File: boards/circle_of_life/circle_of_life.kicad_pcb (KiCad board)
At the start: 2 copper layers, 100 x 82 mm, 110 parts, among them IC1 ESP32-WROOM-32E-N8R2, IC2 TC1262-3.3VDB, IC3 TPS565242DRLR, IC4 LT3922EUFD#PBF, IC5 TXU0101DBVR, J1 Water Pump Connector, J11 LED Connector, J2 Servo Motor Connector, J3 Power Connector, J4 pH Sensor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

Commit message: slightly modified it
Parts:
- moved LED6 204.1 mm to (66.7, 91.8)
- moved LED1 202.9 mm to (66.7, 98.0), turned to 180 degrees
- moved LED7 194.4 mm to (74.5, 91.8)
- moved LED3 189.1 mm to (74.5, 98.0)
- moved LED8 184.9 mm to (82.0, 91.8)
- moved LED9 179.7 mm to (89.5, 98.0), turned to 180 degrees
- moved LED2 178.4 mm to (89.5, 91.8)
- moved LED5 175.5 mm to (81.9, 98.0), turned to 180 degrees
- moved LED10 170.0 mm to (97.2, 98.0), turned to 180 degrees
- moved LED4 164.5 mm to (97.2, 91.8), turned to 180 degrees
- moved J9 53.8 mm to (246.4, 121.0), turned to -90 degrees
- moved IC2 45.8 mm to (194.8, 84.8), turned to 90 degrees
- moved R25 42.8 mm to (187.2, 104.4), turned to 90 degrees
- moved C1 40.0 mm to (193.0, 90.5), turned to 0 degrees
- moved R24 39.3 mm to (189.2, 106.4), turned to 90 degrees
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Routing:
- net +12V: track 0.00 -> 8.67 mm
- net Net-(IC4-PWMTG): track 19.5 -> 25.9 mm
- net ISP: track 9.24 -> 14.0 mm
- net Net-(IC4-CTRL): track 0.50 -> 3.83 mm
- net ISN: track 9.24 -> 11.7 mm
- net INTV: track 5.49 -> 3.71 mm
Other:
- board size 100 x 82 mm -> 100 x 75 mm

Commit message: added usb-uart programmer so that its easier to program :D
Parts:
- added C44: 4.7uF, Capacitor_SMD:C_0805_2012Metric, F.Cu at (222.1, 137.3)
- added C45: 0.1uF, Capacitor_SMD:C_0603_1608Metric, F.Cu at (210.6, 137.1)
- added C46: 4.7uF, Capacitor_SMD:C_0805_2012Metric, F.Cu at (222.1, 140.3)
- added C47: 0.1uF, Capacitor_SMD:C_0603_1608Metric, F.Cu at (210.6, 139.6)
- added D10: LED, LED_SMD:LED_0603_1608Metric, F.Cu at (225.6, 151.4)
- added D8: SP0503BAHTG, SamacSys_Parts:SP0503BAHTG, F.Cu at (220.5, 150.9)
- added D9: LED, LED_SMD:LED_0603_1608Metric, F.Cu at (225.6, 148.8)
- added IC6: CP2102C-A01-GQFN28, SamacSys_Parts:QFN50P500X500X80-29N-D, F.Cu at (216.2, 139.4)
- added P1: USB_C_Plug_USB2.0, Connector_USB:USB_C_Receptacle_GCT_USB4125-xx-x_6P_TopMnt_Horizontal, F.Cu at (234.0, 141.2)
- added Q3: SS8050, Package_TO_SOT_SMD:SOT-23, F.Cu at (215.1, 149.8)
- added Q4: SS8050, Package_TO_SOT_SMD:SOT-23, F.Cu at (215.1, 154.2)
- added R29: 22.1k, Resistor_SMD:R_0603_1608Metric, F.Cu at (210.6, 142.1)
- added R30: 47.5k, Resistor_SMD:R_0603_1608Metric, F.Cu at (210.6, 144.6)
- added R31: 22.1k, Resistor_SMD:R_0603_1608Metric, F.Cu at (210.6, 147.1)
- added R32: 10k, Resistor_SMD:R_0603_1608Metric, F.Cu at (210.6, 149.6)
- added R33: 5.1k, Resistor_SMD:R_0603_1608Metric, F.Cu at (210.6, 152.1)
- added R34: 1k, SamacSys_Parts:RESC1608X55N, F.Cu at (225.5, 154.0)
- added R35: 1k, SamacSys_Parts:RESC1608X55N, F.Cu at (225.5, 156.5)
- added R36: 10k, Resistor_SMD:R_0603_1608Metric, F.Cu at (210.6, 154.6)
- added R37: 10k, Resistor_SMD:R_0603_1608Metric, F.Cu at (210.6, 157.1)
- C24: footprint Capacitor_SMD:C_0603_1608Metric -> SamacSys_Parts:C0603

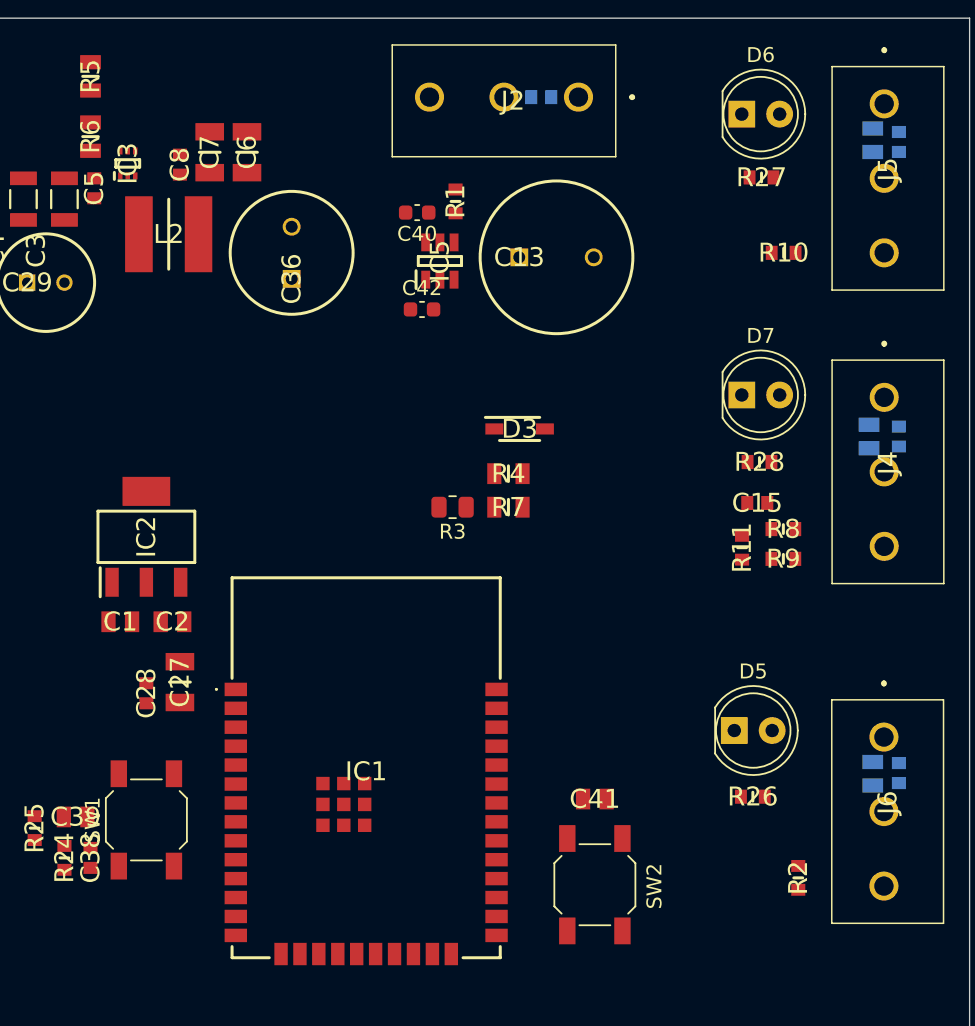
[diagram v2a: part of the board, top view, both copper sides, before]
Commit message: 5V signal routing done
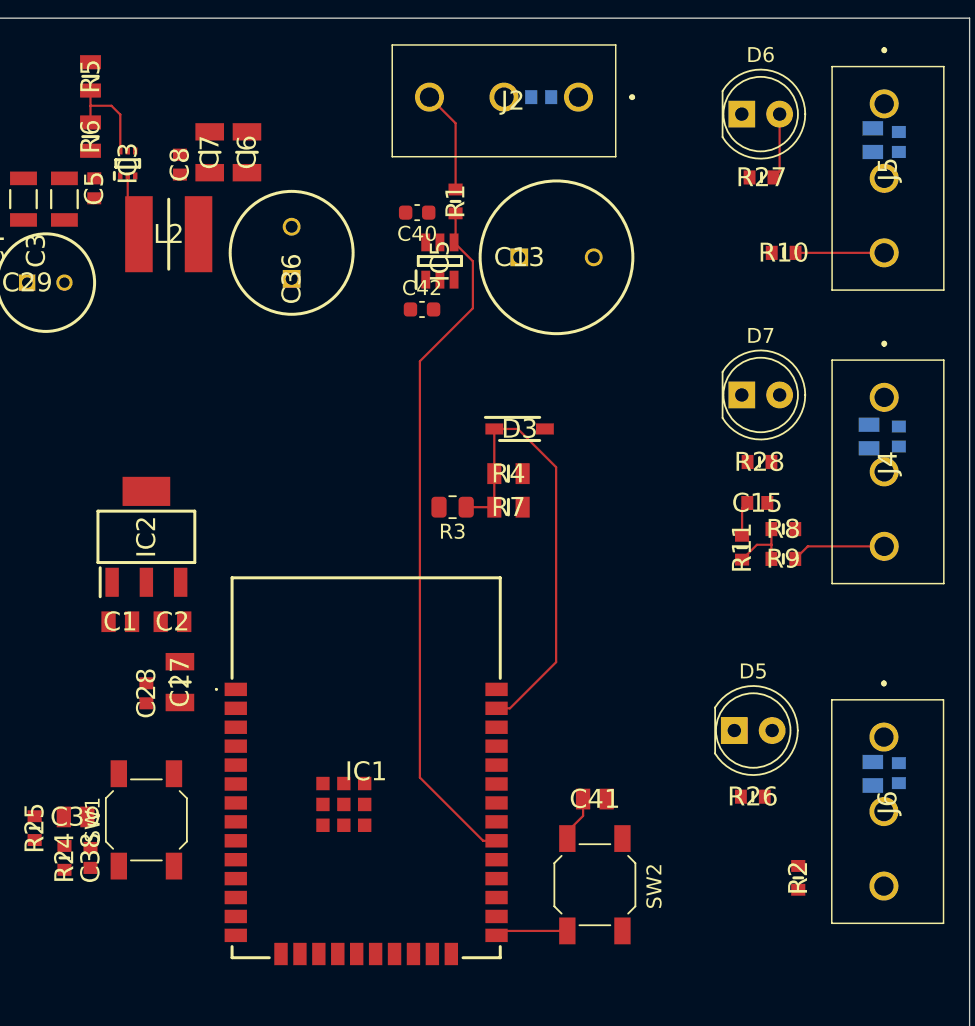
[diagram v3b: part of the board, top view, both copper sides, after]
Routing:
- net SRV_SGN: track 0.00 -> 46.8 mm
- net EN: track 0.00 -> 30.7 mm
- net IO0: track 0.00 -> 7.96 mm
- net Net-(J2-Pin_3): track 0.00 -> 6.92 mm
- net Net-(IC3-FB): track 0.00 -> 6.83 mm
- net PH_SGN: track 0.00 -> 6.32 mm
- net FLOW_SGN: track 0.00 -> 5.95 mm
- net Net-(R11-Pad1): track 0.00 -> 4.45 mm
- net Net-(D6-A): track 0.00 -> 4.42 mm
- net Net-(IC3-SW): track 0.00 -> 4.22 mm
- net PH_SGN_3.3V: track 0.00 -> 2.34 mm

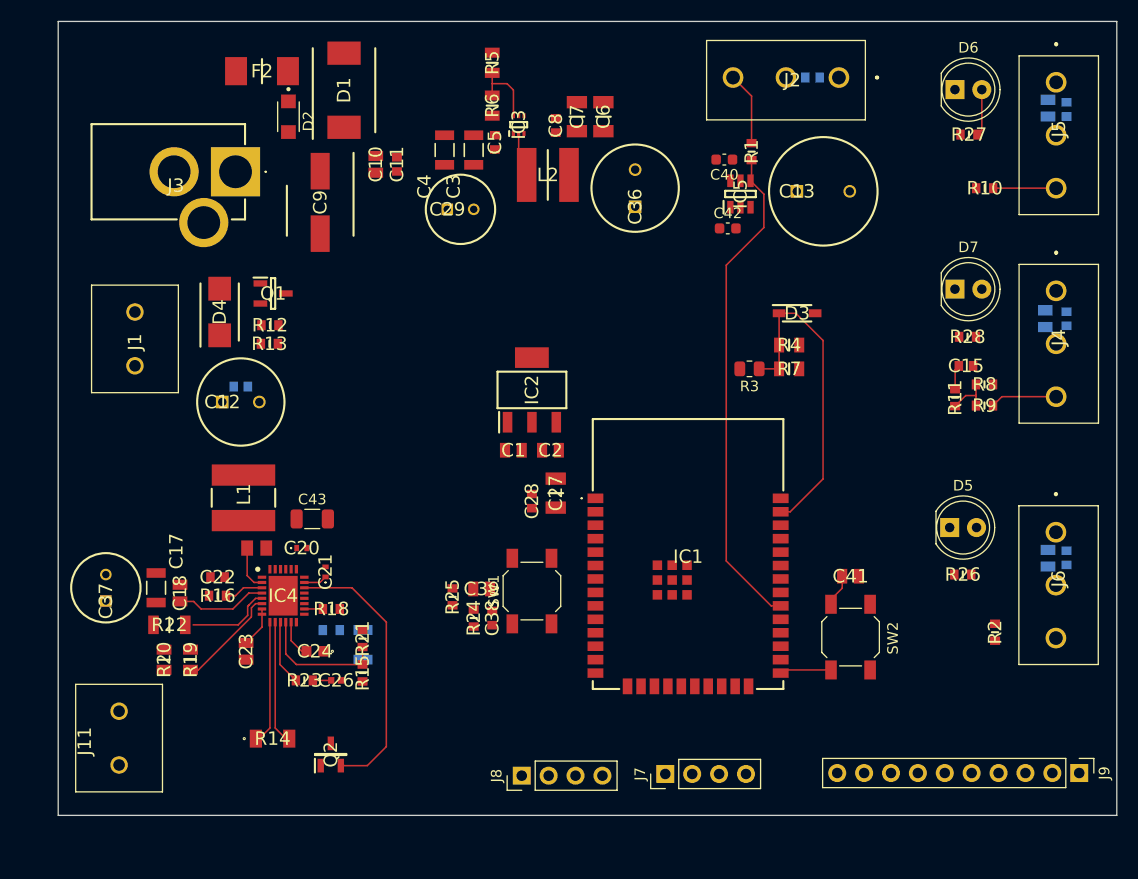
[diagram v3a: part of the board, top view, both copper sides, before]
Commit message: mcu connections started
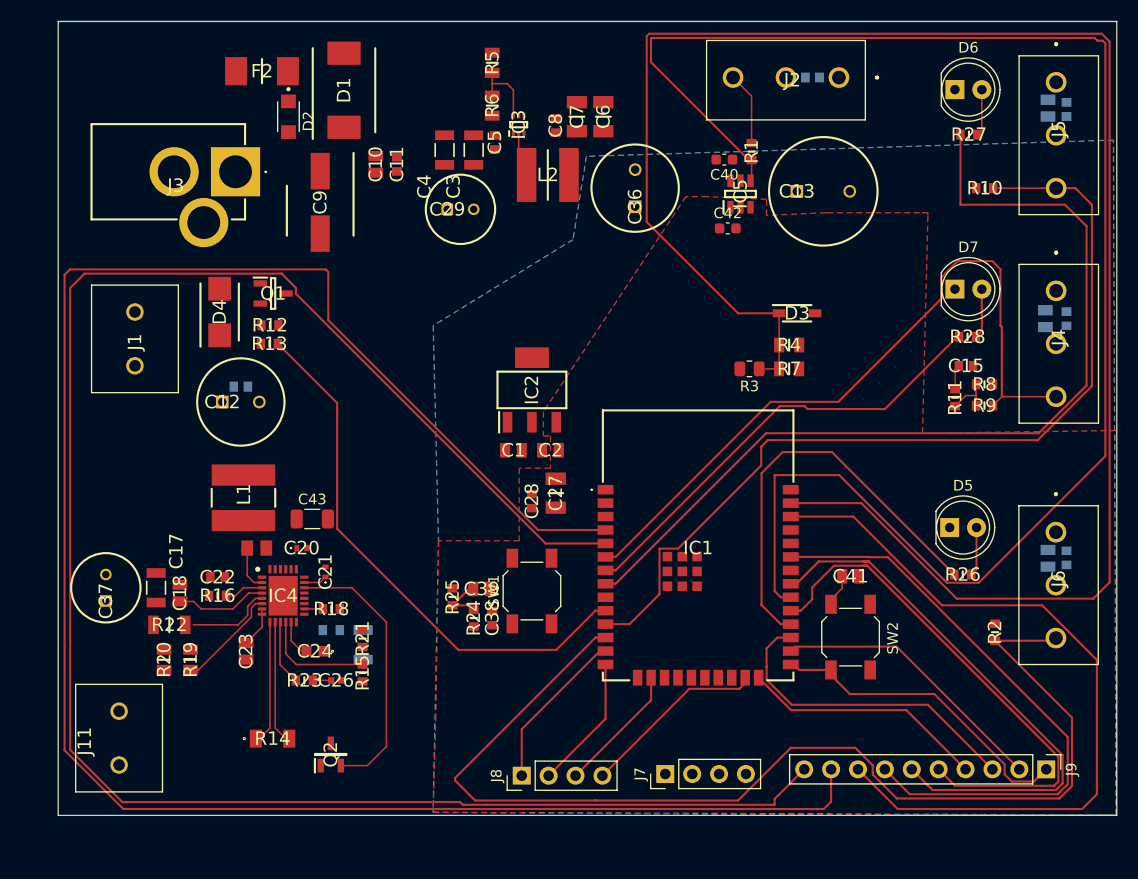
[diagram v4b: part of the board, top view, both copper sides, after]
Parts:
- moved J9 3.14 mm to (243.3, 120.7)
- moved IC1 1.25 mm to (210.5, 99.5)
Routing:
- net SENSOR_VP: track 0.00 -> 188.9 mm
- net SENSOR_VIN: track 0.00 -> 180.0 mm
- net EN: track 30.7 -> 170.5 mm
- net TMP_SGN: track 0.00 -> 106.7 mm
- net SRV_SGN: track 46.8 -> 153.0 mm
- net FLOW_FAULT: track 0.00 -> 87.6 mm
- net FLOW_SGN: track 5.95 -> 85.9 mm
- net IO22: track 0.00 -> 71.9 mm
- net PH_SGN: track 6.32 -> 68.9 mm
- net IO21: track 0.00 -> 56.6 mm
- net IO19: track 0.00 -> 52.9 mm
- net PUMP_SGN: track 0.00 -> 51.4 mm
- net IO5: track 0.00 -> 50.0 mm
- net TEMP_FAULT: track 0.00 -> 42.8 mm
- net PH_FAULT: track 0.00 -> 39.8 mm
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- added copper zone on F.Cu, net +3.3V
- added copper zone on B.Cu, net GND

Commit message: modified layout rip
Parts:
- removed C46: 4.7uF, Capacitor_SMD:C_0805_2012Metric
- removed C47: 0.1uF, Capacitor_SMD:C_0603_1608Metric
- removed J9: Conn_01x10_Pin, Connector_PinHeader_2.54mm:PinHeader_1x10_P2.54mm_Vertical
- removed LED1, LED10, LED3, LED5, LED9: ASMW-LL00-NKM0E, SamacSys_Parts:ASMWLL00NKM0E
- removed LED2, LED4, LED6, LED7, LED8: ASMW-LD00-AGJ0E, SamacSys_Parts:ASMWL300AFH0E
- added D11: TPD1E05U06QDPYRQ1, SamacSys_Parts:DPY_R-PX1SON-N2_, F.Cu at (105.6, 155.7)
- added R38: 0, Resistor_SMD:R_0603_1608Metric, F.Cu at (112.2, 145.7)
- added R39: 0, Resistor_SMD:R_0603_1608Metric, F.Cu at (113.9, 145.7)
- C22, R16, R2: moved to B.Cu
- C24: footprint SamacSys_Parts:C0603 -> Capacitor_SMD:C_0603_1608Metric
- D8: value SP0503BAHTG -> TPD1E05U06QDPYRQ1; footprint SamacSys_Parts:SP0503BAHTG -> SamacSys_Parts:DPY_R-PX1SON-N2_
- P1: footprint Connector_USB:USB_C_Receptacle_GCT_USB4125-xx-x_6P_TopMnt_Horizontal -> Connector_USB:USB_C_Receptacle_HRO_TYPE-C-31-M-12
- moved J5 192.4 mm to (110.6, 194.2), turned to 0 degrees
- moved J2 191.5 mm to (92.0, 194.3), turned to 0 degrees
- moved C32 190.9 mm to (112.8, 195.8), turned to 180 degrees
- moved C14 188.1 mm to (94.5, 194.3), turned to 180 degrees
- moved C33 187.0 mm to (112.7, 191.8), turned to 180 degrees
- moved J4 180.2 mm to (92.1, 171.9), turned to 90 degrees
- moved C31 179.1 mm to (91.1, 169.3), turned to -90 degrees
- moved D6 178.5 mm to (110.1, 184.3), turned to -90 degrees
- moved R27 175.7 mm to (114.3, 187.4), turned to -90 degrees
- moved C30 175.7 mm to (93.1, 169.3), turned to -90 degrees
- moved C13 170.7 mm to (96.0, 183.6), turned to 180 degrees
- moved R1 170.0 mm to (100.2, 187.3), turned to -90 degrees
- moved R10 169.5 mm to (119.4, 187.3), turned to 90 degrees
- moved C40 165.5 mm to (102.8, 186.6), turned to 0 degrees
- moved D7 164.5 mm to (101.6, 172.1), turned to 180 degrees
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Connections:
- D8 pad 1: GND -> D+
- D8 pad 2: D- -> GND
- IC1 pad 10: PUMP_SGN -> FLOW_SGN
- IC1 pad 11: FLOW_SGN -> PUMP_SGN
- IC1 pad 24: IO2 -> unconnected-(IC1-IO2-Pad24)
- IC1 pad 26: IO4 -> unconnected-(IC1-IO4-Pad26)
- IC1 pad 27: IO16 -> unconnected-(IC1-IO16-Pad27)
- IC1 pad 29: IO5 -> unconnected-(IC1-IO5-Pad29)
- IC1 pad 30: SRV_SGN -> unconnected-(IC1-IO18-Pad30)
- IC1 pad 31: IO19 -> unconnected-(IC1-IO19-Pad31)
- IC1 pad 33: IO21 -> unconnected-(IC1-IO21-Pad33)
- IC1 pad 34: RX -> RXD0
- IC1 pad 35: TX -> TXD0
- IC1 pad 36: IO22 -> SRV_SGN_3.3V
- IC1 pad 6: PH_SGN -> FLOW_FAULT
- IC1 pad 8: FLOW_FAULT -> PH_SGN
- J7 pad 2: TX -> TXD0
- J7 pad 3: RX -> RXD0
- P1 pad A9: Net-(P1-VBUS-PadA4) -> +5V
- P1 pad B9: Net-(P1-VBUS-PadA4) -> +5V
- R29 pad 1: Net-(P1-VBUS-PadA4) -> +5V
- R31 pad 2: VDD -> +3.3V
- SW1 pad 1: GND -> unconnected-(SW1-Pad1)
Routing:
- net SENSOR_VP: track 188.9 -> 0.16 mm
- net SENSOR_VIN: track 180.0 -> 0.00 mm
- net SRV_SGN: track 153.0 -> 1.99 mm
- net GND: track 0.00 -> 149.1 mm, vias 0 -> 67
- net EN: track 170.5 -> 74.1 mm, vias 0 -> 4
- net TMP_SGN: track 106.7 -> 11.6 mm, vias 0 -> 1
- net IO22: track 71.9 -> 0.00 mm
- net +3.3V: track 0.00 -> 68.3 mm, vias 0 -> 2
- net SRV_SGN_3.3V: track 0.00 -> 60.2 mm, vias 0 -> 2
- net IO21: track 56.6 -> 0.00 mm
- net MCU_EN: track 5.19 -> 60.9 mm, vias 0 -> 2
- net IO19: track 52.9 -> 0.00 mm
- net PWM_DIM: track 0.63 -> 53.2 mm, vias 0 -> 4
- net +5V: track 0.00 -> 51.1 mm
- net ISP: track 14.0 -> 64.0 mm
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- added copper zone on F.Cu, net +12V
- added copper zone on F.Cu, net +5V
- added copper zone on F.Cu, net GND
- added copper zone on F.Cu, net ISP
- added copper zone on F.Cu, net LEDS
- added copper zone on F.Cu, net Net-(D1-A)
- added copper zone on F.Cu, net SW
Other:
- board size 100 x 75 mm -> 86.6 x 96.4 mm

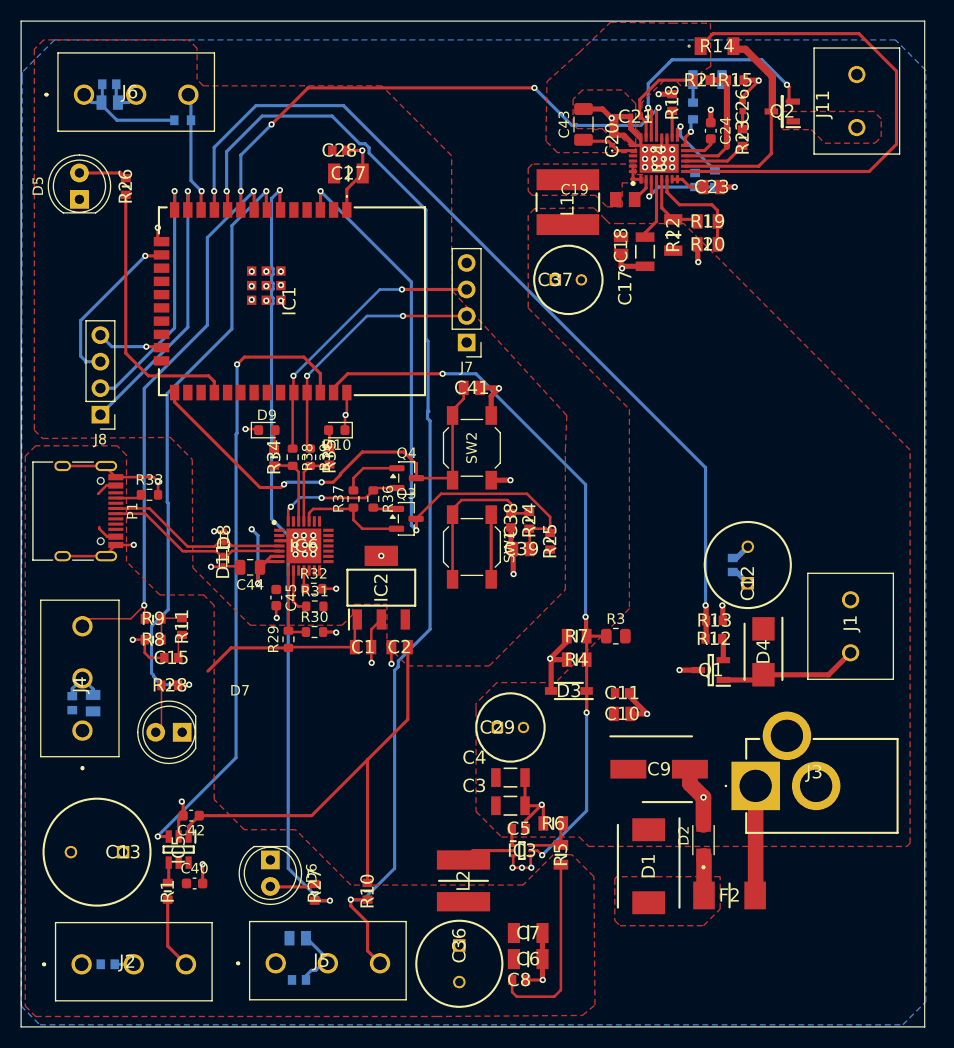
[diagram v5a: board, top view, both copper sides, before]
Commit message: modified current sensor cause i just couldnt leave it like that
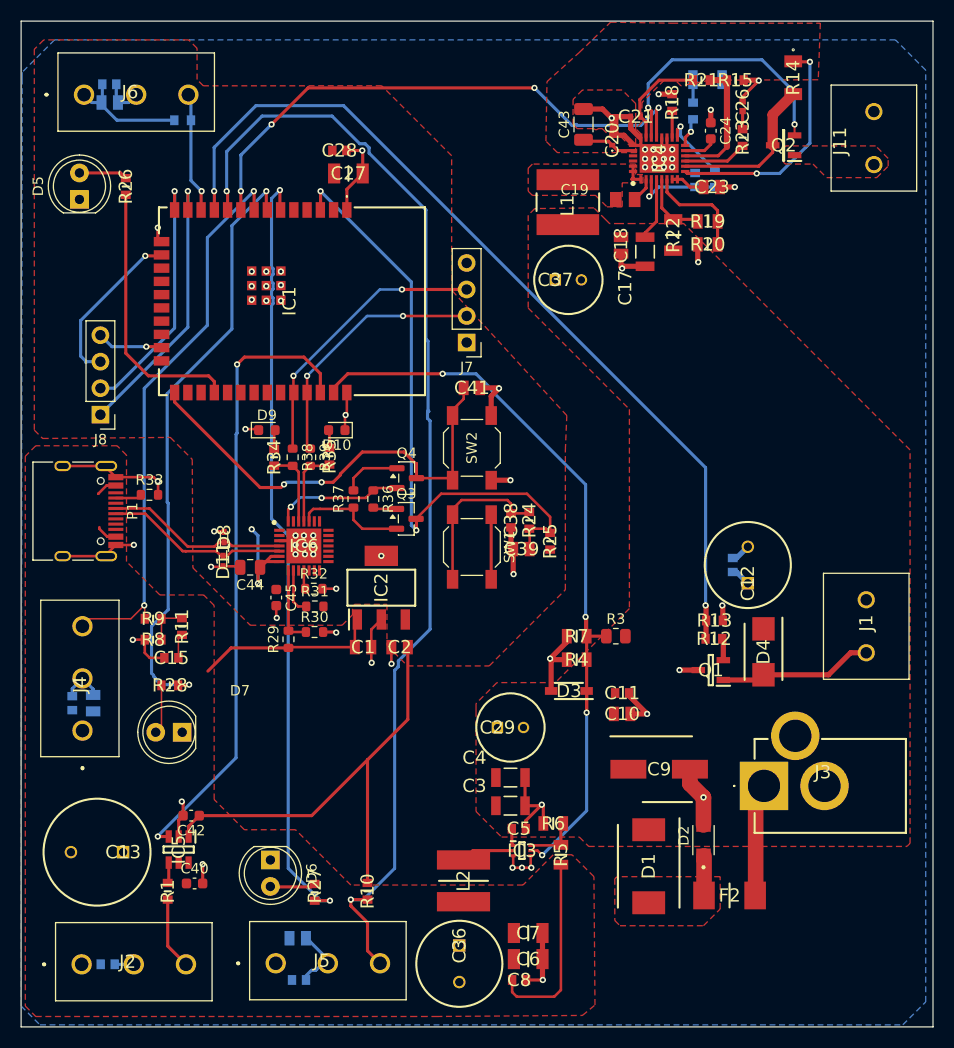
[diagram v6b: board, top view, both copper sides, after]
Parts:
- moved R14 7.90 mm to (160.2, 109.3), turned to -90 degrees
- moved J11 3.91 mm to (167.9, 117.6)
- moved Q2 3.24 mm to (159.3, 115.8)
- moved J1 1.50 mm to (167.2, 159.4)
- moved J3 0.80 mm to (157.4, 177.2)
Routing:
- net ISP: track 64.0 -> 37.6 mm, vias 0 -> 2
- net ISN: track 21.0 -> 15.3 mm
- net Net-(IC4-PWMTG): track 22.3 -> 25.7 mm
- net Net-(D4-A): track 13.3 -> 14.8 mm
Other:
- board size 86.6 x 96.4 mm -> 87.4 x 96.4 mm
